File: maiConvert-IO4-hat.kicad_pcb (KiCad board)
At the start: 2 copper layers, 77 parts, among them J1 CN3 - From IO4, J10 1P B7, J11 1P B8, J12 2P B1, J13 2P B2, J14 2P B3, J15 2P B4, J16 2P B5, J17 2P B6, J18 2P B7, J19 2P B8, J2 CN9 - From IO4, J20 1P SELECT BUTTON, J21 2P SELECT BUTTON, J22 12V input, J23 BILLBOARD LED L, J24 BILLBOARD LED R, J25 1P CODE READER LED, J26 2P CODE READER LED, J27 COIN METER, J28 COIN LOCKOUT, J29 CAMERA LED RED, J3 CN3 - To Harness, J30 CAMERA LED WARM, J31 TEST BUTTON, J32 COIN BUTTON, J33 SERVICE BUTTON, J4 1P B1, J5 1P B2, J6 1P B3, J7 1P B4, J8 1P B5, J9 1P B6, SW1 TEST, SW10 SW_Push_Open, SW11 SW_Push_Open, SW12 SW_Push_Open, SW13 SW_Push_Open, SW14 SW_Push_Open, SW15 SW_Push_Open, SW16 SW_Push_Open, SW17 SW_Push_Open, SW18 SW_Push_Open, SW19 SW_Push_Open, SW2 COIN, SW20 SW_Push_Open, SW21 SW_Push_Open, SW3 SERVICE, SW4 1P SELECT BTN, SW5 2P SELECT BTN, SW6 SW_Push_Open, SW7 SW_Push_Open, SW8 SW_Push_Open, SW9 SW_Push_Open

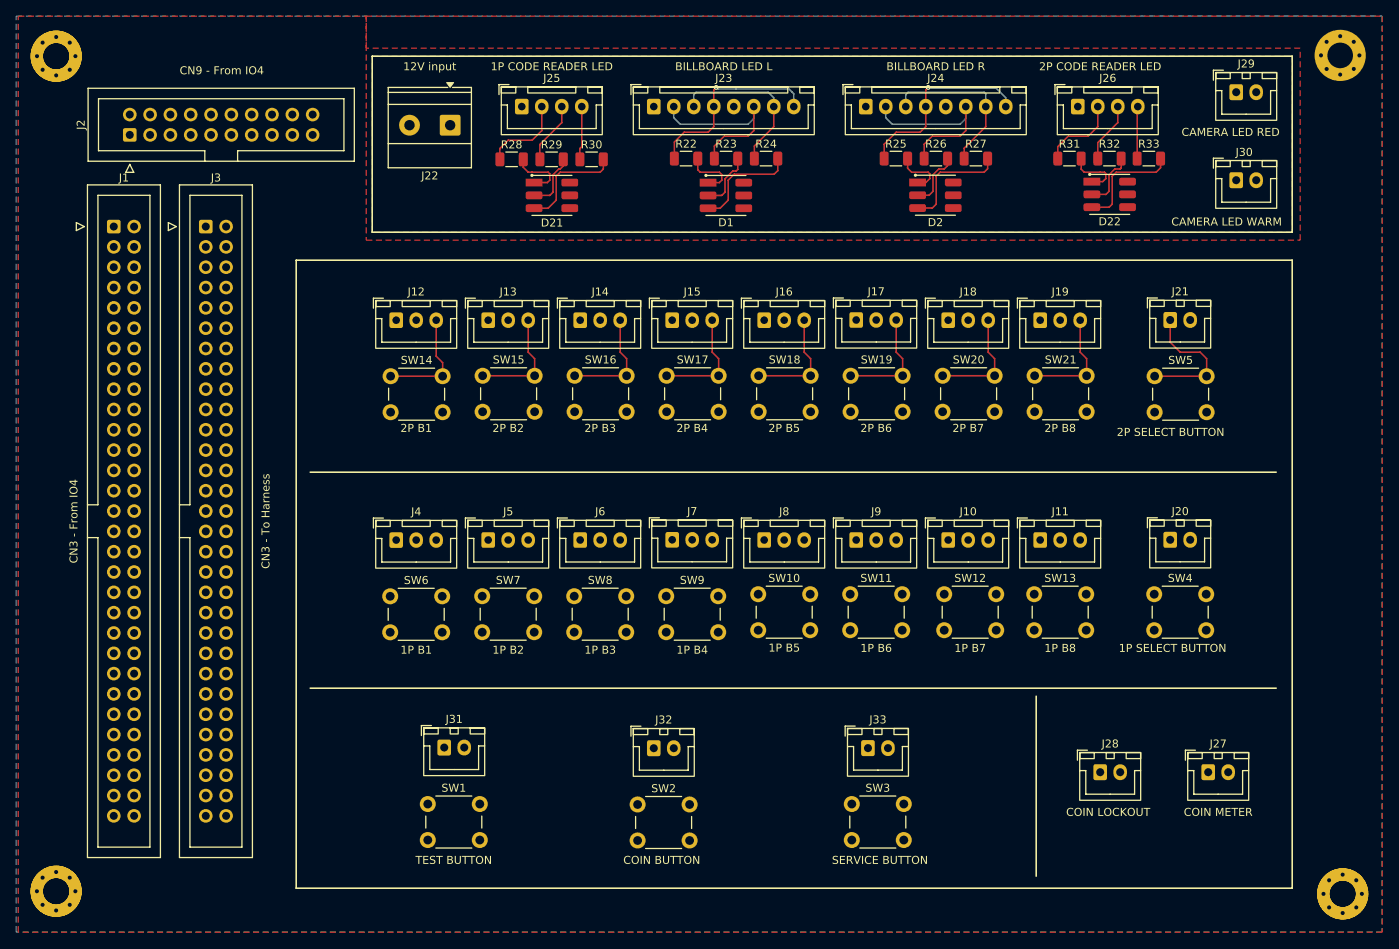
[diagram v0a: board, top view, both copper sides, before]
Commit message: Finish mapping PCB
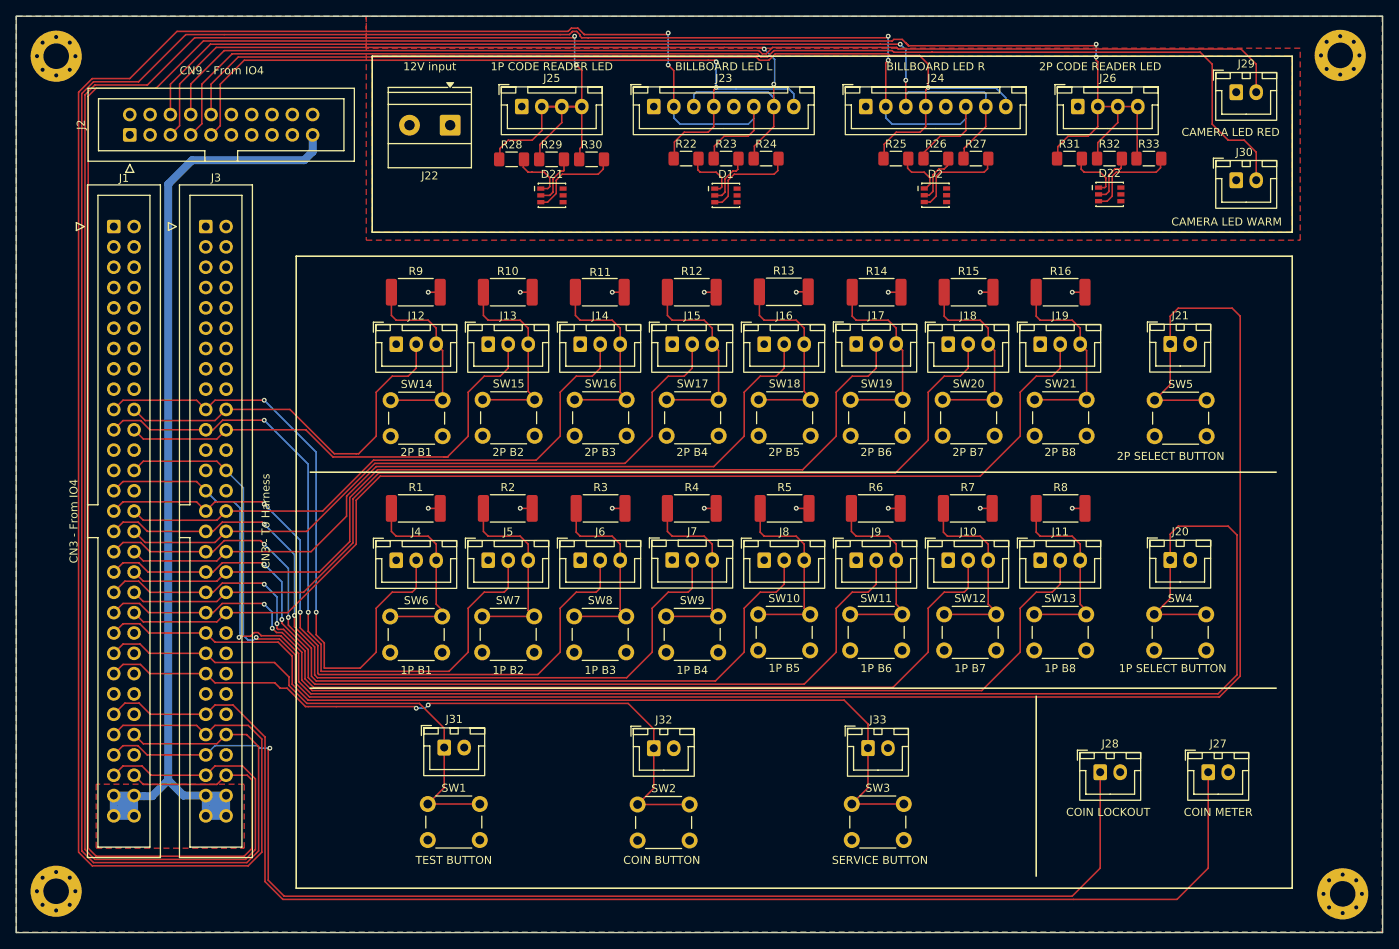
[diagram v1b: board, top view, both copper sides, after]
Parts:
- removed ? (x3): , 
- added R1: 50, Resistor_SMD:R_2512_6332Metric_Pad1.40x3.35mm_HandSolder, F.Cu at (109.5, 96.0)
- added R10: 50, Resistor_SMD:R_2512_6332Metric_Pad1.40x3.35mm_HandSolder, F.Cu at (121.0, 69.0)
- added R11: 50, Resistor_SMD:R_2512_6332Metric_Pad1.40x3.35mm_HandSolder, F.Cu at (132.4, 69.0)
- added R12: 50, Resistor_SMD:R_2512_6332Metric_Pad1.40x3.35mm_HandSolder, F.Cu at (143.9, 69.0)
- added R13: 50, Resistor_SMD:R_2512_6332Metric_Pad1.40x3.35mm_HandSolder, F.Cu at (155.4, 69.0)
- added R14: 50, Resistor_SMD:R_2512_6332Metric_Pad1.40x3.35mm_HandSolder, F.Cu at (167.1, 69.0)
- added R15: 50, Resistor_SMD:R_2512_6332Metric_Pad1.40x3.35mm_HandSolder, F.Cu at (178.6, 69.0)
- added R16: 50, Resistor_SMD:R_2512_6332Metric_Pad1.40x3.35mm_HandSolder, F.Cu at (190.1, 69.0)
- added R2: 50, Resistor_SMD:R_2512_6332Metric_Pad1.40x3.35mm_HandSolder, F.Cu at (121.0, 96.0)
- added R3: 50, Resistor_SMD:R_2512_6332Metric_Pad1.40x3.35mm_HandSolder, F.Cu at (132.6, 96.0)
- added R4: 50, Resistor_SMD:R_2512_6332Metric_Pad1.40x3.35mm_HandSolder, F.Cu at (143.9, 96.0)
- added R5: 50, Resistor_SMD:R_2512_6332Metric_Pad1.40x3.35mm_HandSolder, F.Cu at (155.6, 96.0)
- added R6: 50, Resistor_SMD:R_2512_6332Metric_Pad1.40x3.35mm_HandSolder, F.Cu at (166.9, 96.0)
- added R7: 50, Resistor_SMD:R_2512_6332Metric_Pad1.40x3.35mm_HandSolder, F.Cu at (178.4, 96.0)
- added R8: 50, Resistor_SMD:R_2512_6332Metric_Pad1.40x3.35mm_HandSolder, F.Cu at (190.1, 96.0)
- added R9: 50, Resistor_SMD:R_2512_6332Metric_Pad1.40x3.35mm_HandSolder, F.Cu at (109.5, 69.0)
- D1, D2, D21, D22: footprint FabricationParts:LED_RGB_PLCC6_5050_XL5050RGBC -> LED_RGB_Wurth:LED_RGB_Wurth_WL-SFTW_150352M173300
- R22, R23, R24, R25, R26, R27, R28, R29, R30, R31, R32, R33: value 1kΩ -> 1k; footprint Resistor_SMD:R_1206_3216Metric -> Resistor_SMD:R_1206_3216Metric_Pad1.30x1.75mm_HandSolder
- SW10: value SW_Push_Open -> 1P B5 BTN
- SW11: value SW_Push_Open -> 1P B6 BTN
- SW12: value SW_Push_Open -> 1P B7 BTN
- SW13: value SW_Push_Open -> 1P B8 BTN
- SW14: value SW_Push_Open -> 2P B1 BTN
- SW15: value SW_Push_Open -> 2P B2 BTN
- SW16: value SW_Push_Open -> 2P B3 BTN
- SW17: value SW_Push_Open -> 2P B4 BTN
- SW18: value SW_Push_Open -> 2P B5 BTN
- SW19: value SW_Push_Open -> 2P B6 BTN
- SW20: value SW_Push_Open -> 2P B7 BTN
- SW21: value SW_Push_Open -> 2P B8 BTN
- SW6: value SW_Push_Open -> 1P B1 BTN
- SW7: value SW_Push_Open -> 1P B2 BTN
- SW8: value SW_Push_Open -> 1P B3 BTN
- SW9: value SW_Push_Open -> 1P B4 BTN
- moved J12 3.00 mm to (107.0, 75.5)
- moved J13 3.00 mm to (118.5, 75.5)
- moved J14 3.00 mm to (130.0, 75.5)
- moved J15 3.00 mm to (141.5, 75.5)
- moved J16 3.00 mm to (153.0, 75.5)
- moved J17 3.00 mm to (164.5, 75.5)
- moved J18 3.00 mm to (176.0, 75.5)
- moved J19 3.00 mm to (187.5, 75.5)
- moved J21 3.00 mm to (203.8, 75.5)
- moved SW14 3.00 mm to (106.3, 82.5)
- moved SW15 3.00 mm to (117.8, 82.4)
- moved SW16 3.00 mm to (129.3, 82.4)
- moved SW17 3.00 mm to (140.8, 82.4)
- moved SW18 3.00 mm to (152.3, 82.4)
- moved SW19 3.00 mm to (163.8, 82.4)
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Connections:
- D1 pad 2: Net-(D1-R-) -> +12V
- D1 pad 3: Net-(D1-G-) -> Net-(D1-R-)
- D1 pad 5: +12V -> Net-(D1-G-)
- D2 pad 2: Net-(D2-R-) -> +12V
- D2 pad 3: Net-(D2-G-) -> Net-(D2-R-)
- D2 pad 5: +12V -> Net-(D2-G-)
- D21 pad 2: Net-(D21-R-) -> +12V
- D21 pad 3: Net-(D21-G-) -> Net-(D21-R-)
- D21 pad 5: +12V -> Net-(D21-G-)
- D22 pad 2: Net-(D22-R-) -> +12V
- D22 pad 3: Net-(D22-G-) -> Net-(D22-R-)
- D22 pad 5: +12V -> Net-(D22-G-)
- SW10 pad 2: GND -> +5V
- SW11 pad 2: GND -> +5V
- SW12 pad 2: GND -> +5V
- SW13 pad 2: GND -> +5V
- SW14 pad 2: GND -> +5V
- SW15 pad 2: GND -> +5V
- SW16 pad 2: GND -> +5V
- SW17 pad 2: GND -> +5V
- SW18 pad 2: GND -> +5V
- SW19 pad 2: GND -> +5V
- SW20 pad 2: GND -> +5V
- SW21 pad 2: GND -> +5V
- SW4 pad 1: GND -> /1P SELECT BUTTON
- SW4 pad 2: /1P SELECT BUTTON -> GND
- SW6 pad 2: GND -> +5V
- SW7 pad 2: GND -> +5V
- SW8 pad 2: GND -> +5V
- SW9 pad 2: GND -> +5V
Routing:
- net /2P CODE READER LED: track 24.1 -> 306.9 mm, vias 0 -> 2
- net /BILLBOARD LED R RED: track 24.2 -> 285.4 mm, vias 0 -> 2
- net /BILLBOARD LED L RED: track 23.8 -> 265.0 mm, vias 0 -> 2
- net /1P CODE READER LED: track 24.9 -> 254.0 mm, vias 0 -> 2
- net /2P SELECT BUTTON: track 16.9 -> 237.6 mm, vias 0 -> 1
- net /1P SELECT BUTTON: track 0.00 -> 209.2 mm, vias 0 -> 1
- net /COIN METER: track 0.00 -> 172.7 mm
- net /COIN LOCKOUT: track 0.00 -> 155.9 mm, vias 0 -> 1
- net /CAMERA LED WARM: track 0.00 -> 153.9 mm
- net /CAMERA LED RED: track 0.00 -> 143.6 mm
- net /Isolated IO4 12V: track 0.00 -> 141.6 mm
- net /1P BUTTON 8: track 0.00 -> 139.2 mm, vias 0 -> 2
- net /2P BUTTON 8: track 0.00 -> 138.8 mm
- net /1P BUTTON 7: track 0.00 -> 130.7 mm, vias 0 -> 2
- net /2P BUTTON 7: track 0.00 -> 126.6 mm
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- added copper zone on F.Cu, net /Isolated IO4 12V
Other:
- board outline added: 170.8 x 114.6 mm
